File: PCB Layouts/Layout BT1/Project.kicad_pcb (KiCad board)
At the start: 2 copper layers, 45 x 20 mm, 21 parts, among them J1 Conn_01x04

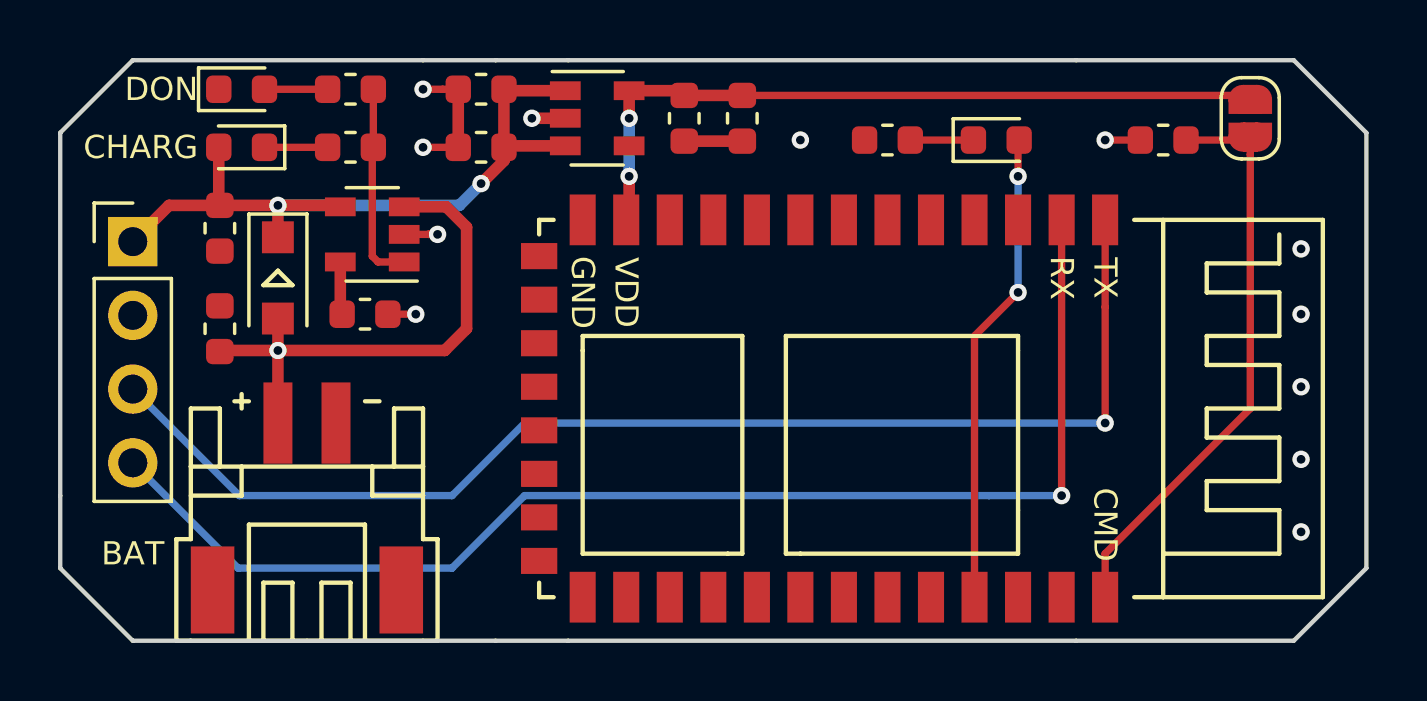
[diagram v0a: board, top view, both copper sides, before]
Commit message: Finalized silkscreen for Layout BT1 and generated gerbers
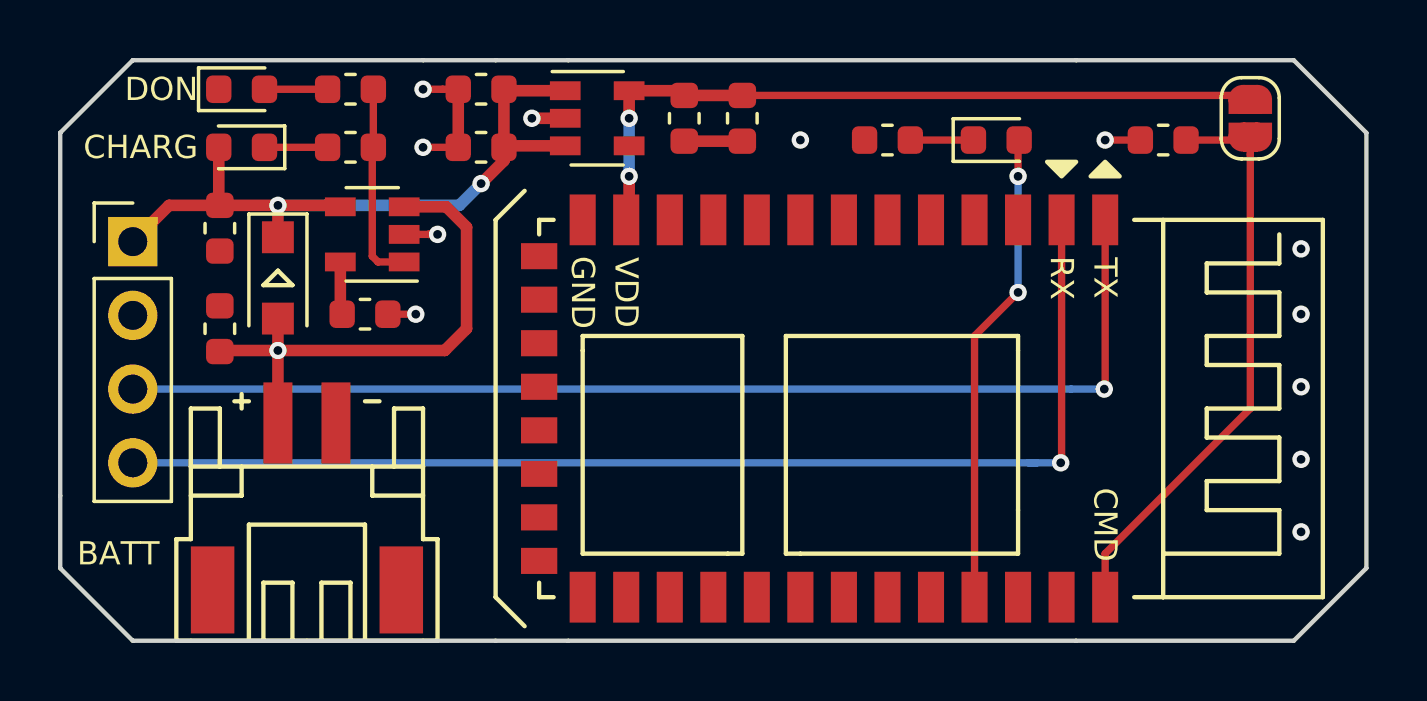
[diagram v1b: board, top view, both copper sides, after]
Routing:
- net TX: track 43.1 -> 39.3 mm
- net RX: track 44.0 -> 40.9 mm
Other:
- board text added: "3.3"
- board text added: "BATT"
- board text added: "CHG"
- board text added: "CMD"
- board text removed: "BAT"
